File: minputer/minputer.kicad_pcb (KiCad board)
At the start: 4 copper layers, 150 x 90 mm, 116 parts, among them J1 Conn_02x10_Odd_Even, J2 Conn_01x03_Male, J3 Conn_01x02_Male, J4 Conn_02x20_Odd_Even, J5 Conn_02x05_Odd_Even, P1 USB_C_Plug_USB2.0, SW1 SW_Push, U1 DS1318, U10 16C2552_PLCC, U11 CP2102N-Axx-xQFN20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

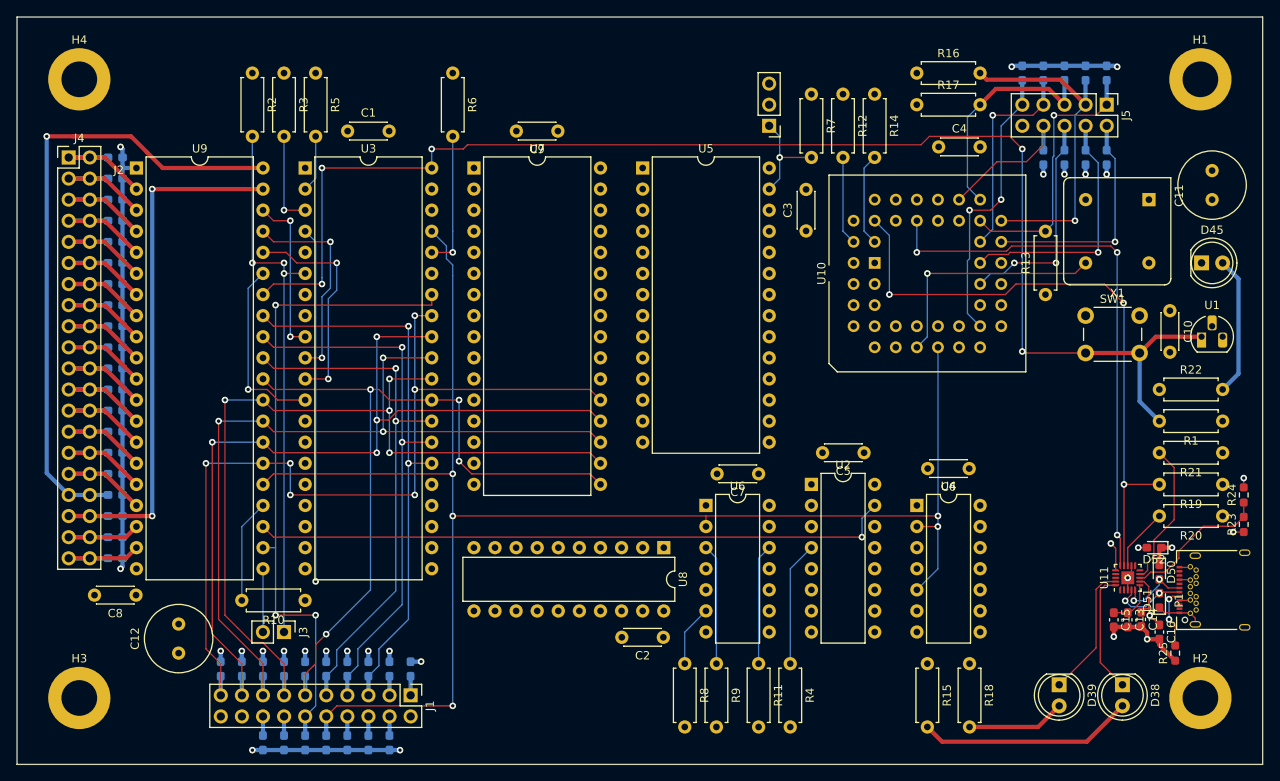
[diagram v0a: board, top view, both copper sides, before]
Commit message: Route BUS connector
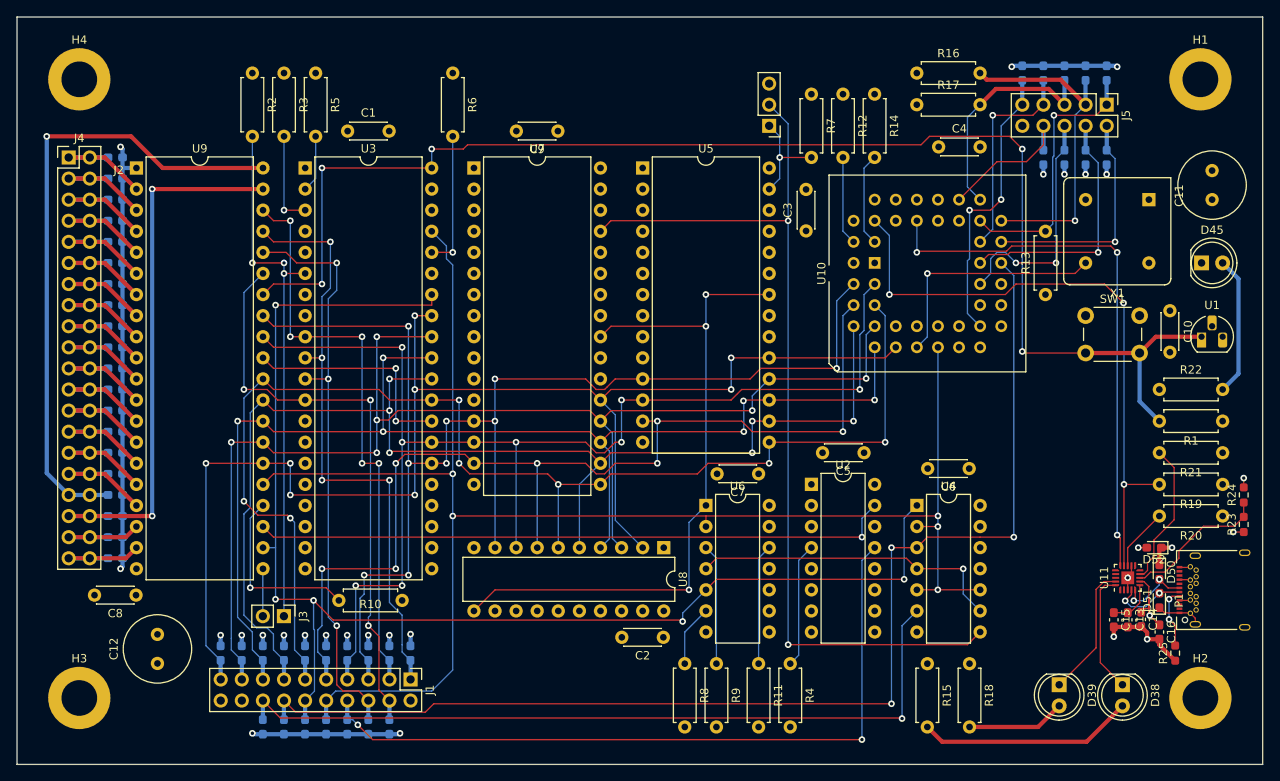
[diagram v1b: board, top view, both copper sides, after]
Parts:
- moved R10 11.7 mm to (71.4, 95.2)
- moved C12 2.84 mm to (41.9, 102.8)
- moved J1 1.91 mm to (72.4, 104.8)
- moved D1 1.91 mm to (49.5, 101.6)
- moved D10 1.91 mm to (72.4, 101.6)
- moved D11 1.91 mm to (54.6, 110.5)
- moved D12 1.91 mm to (57.1, 110.5)
- moved D13 1.91 mm to (59.7, 110.5)
- moved D14 1.91 mm to (62.2, 110.5)
- moved D15 1.91 mm to (64.8, 110.5)
- moved D16 1.91 mm to (67.3, 110.5)
- moved D17 1.91 mm to (69.8, 110.5)
- moved D2 1.91 mm to (52.1, 101.6)
- moved D3 1.91 mm to (54.6, 101.6)
- moved D4 1.91 mm to (57.1, 101.6)
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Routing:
- net /RDB: track 2.30 -> 143.4 mm, vias 0 -> 3
- net /~{WE}: track 0.00 -> 112.9 mm, vias 0 -> 2
- net /WRB: track 2.30 -> 93.8 mm, vias 0 -> 1
- net /D0: track 67.3 -> 156.1 mm, vias 2 -> 9
- net /D2: track 63.7 -> 151.8 mm, vias 2 -> 9
- net /AUXCSB: track 2.30 -> 89.0 mm, vias 0 -> 2
- net /D1: track 65.5 -> 151.2 mm, vias 2 -> 8
- net /PHI1: track 0.00 -> 84.2 mm, vias 0 -> 3
- net /RWB: track 78.8 -> 160.9 mm, vias 3 -> 5
- net GND: track 126.2 -> 207.8 mm
- net /D3: track 92.6 -> 155.1 mm, vias 4 -> 7
- net /D7: track 106.5 -> 162.5 mm, vias 6 -> 8
- net /D6: track 103.1 -> 153.8 mm, vias 4 -> 6
- net /D5: track 99.3 -> 149.2 mm, vias 3 -> 6
- net /D4: track 101.8 -> 150.6 mm, vias 4 -> 6
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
